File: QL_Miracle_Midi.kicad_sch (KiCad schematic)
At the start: 32 parts, among them J1 QL_cartridge_ROM, J2 DIN-5, J3 DIN-5, J4 DIN-5, U1 Z80CPU, U10 74LS74, U2 6264, U3 74LS374, U4 74LS374, U5 74LS10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

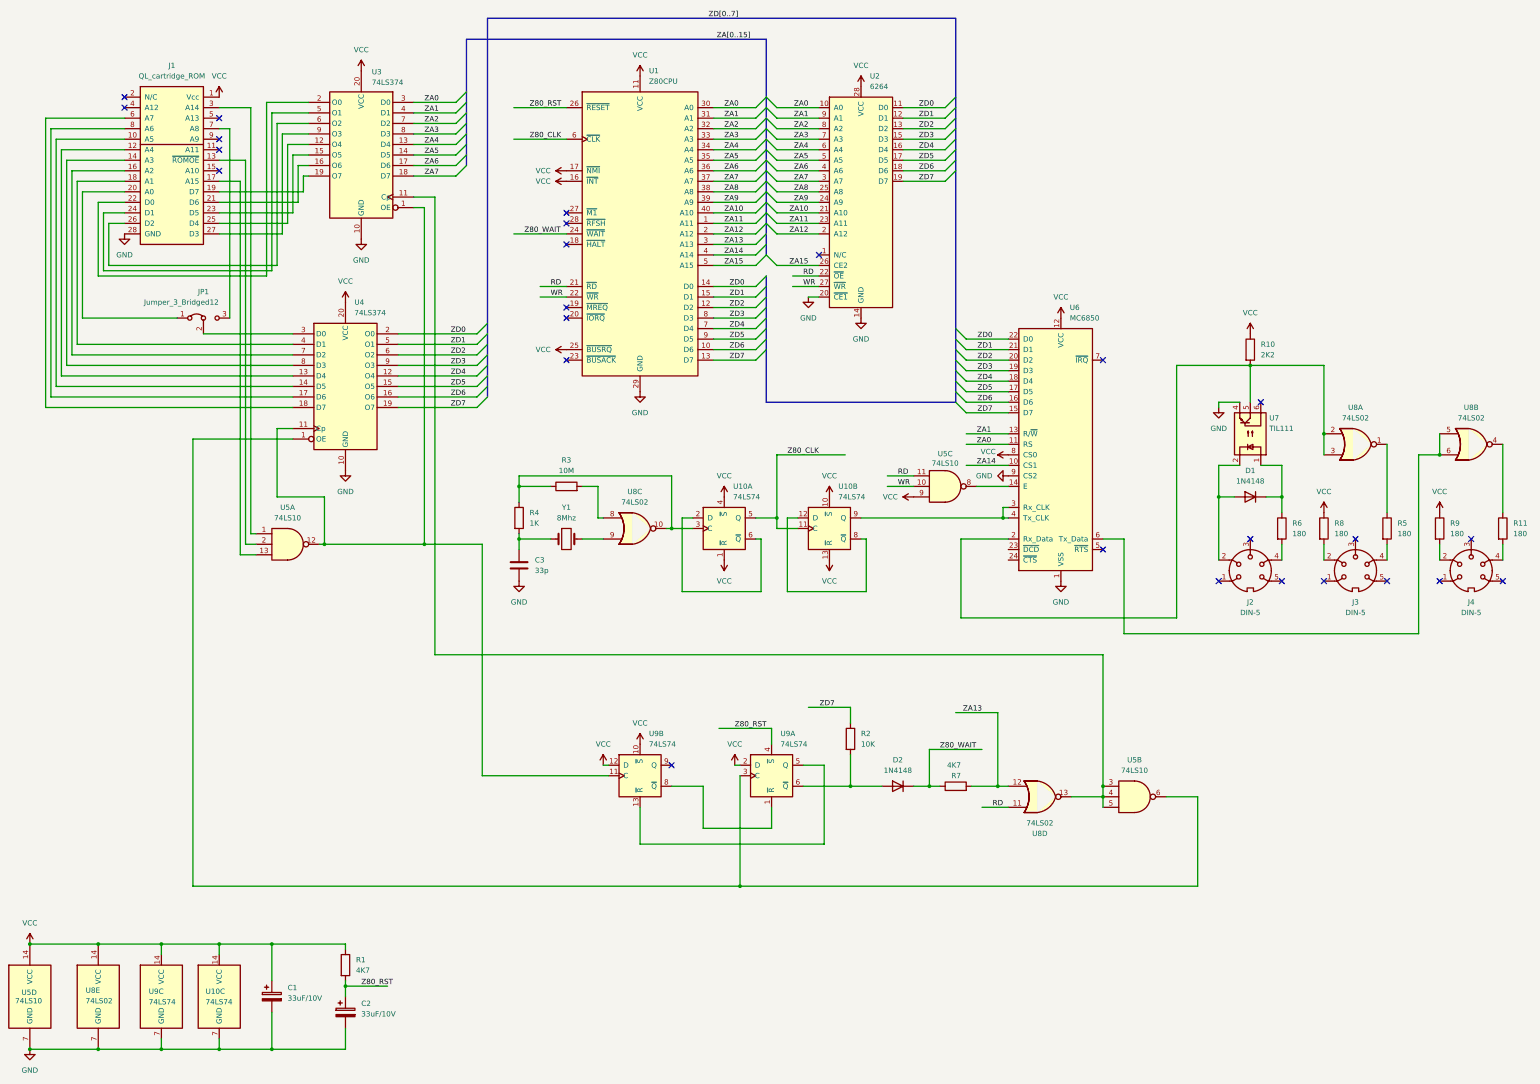
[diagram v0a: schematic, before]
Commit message: now based on real PCB
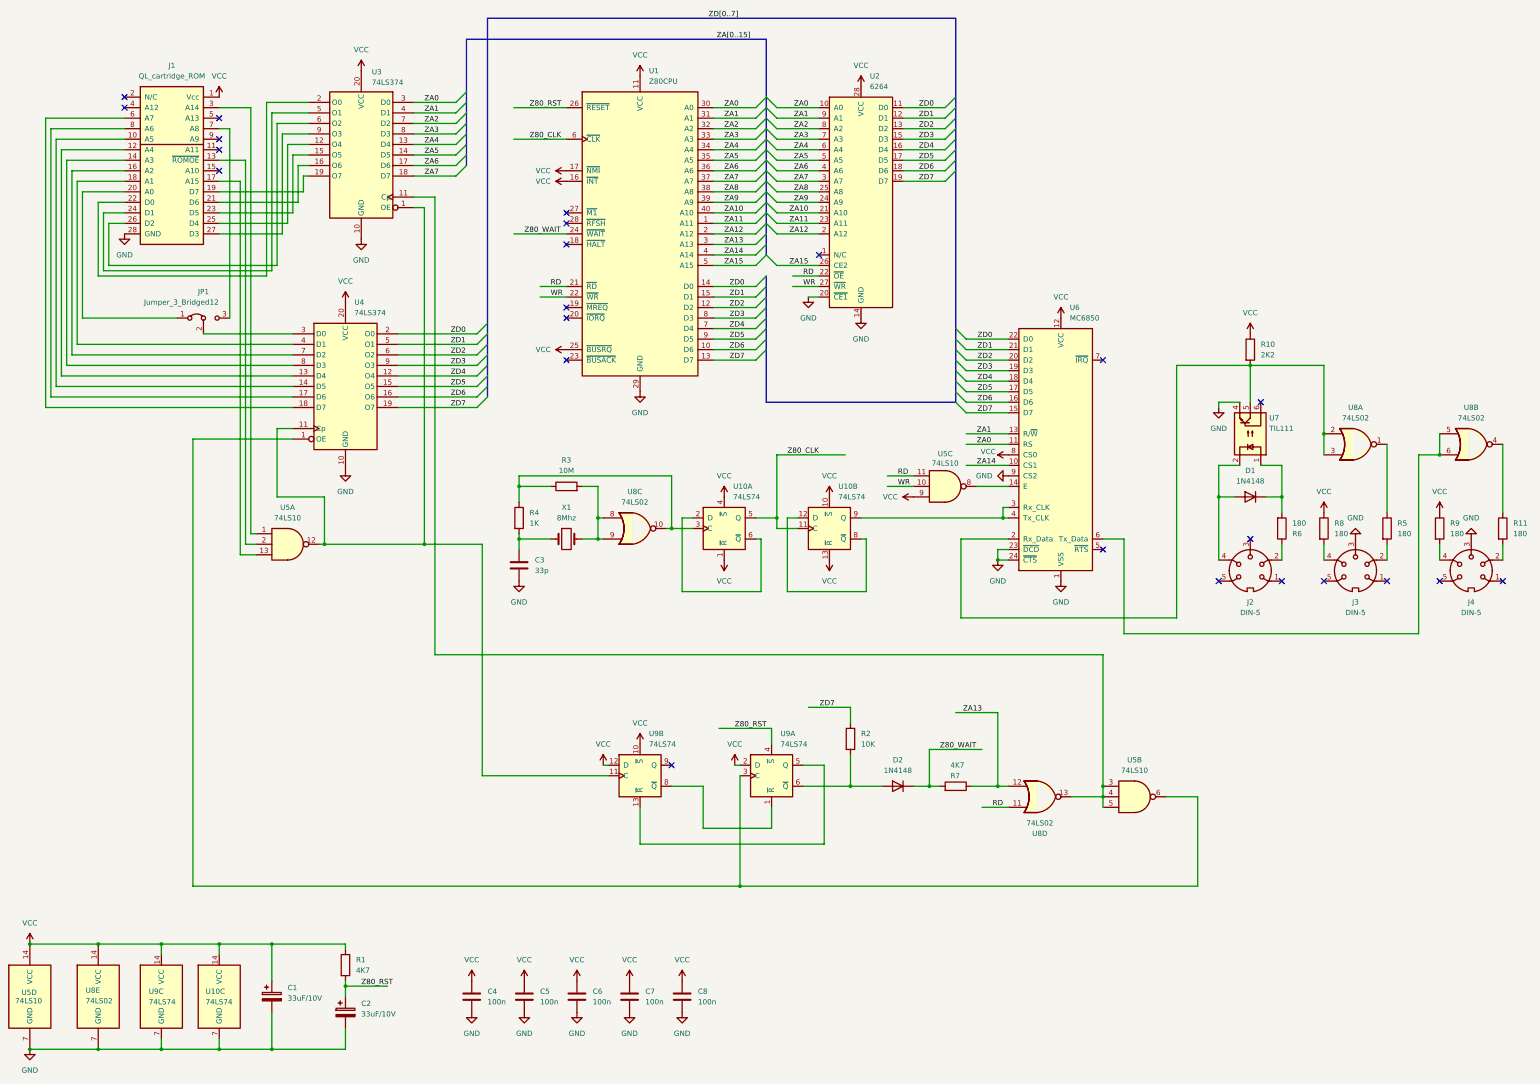
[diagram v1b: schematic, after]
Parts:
- added C4, C5, C6, C7, C8: 100n, Capacitor_THT:C_Disc_D4.3mm_W1.9mm_P5.00mm, symbol Device:C
- C1, C2: footprint Capacitor_THT:CP_Radial_D5.0mm_P2.50mm -> Capacitor_THT:CP_Axial_L11.0mm_D5.0mm_P18.00mm_Horizontal
- C3: footprint Capacitor_THT:C_Disc_D4.3mm_W1.9mm_P5.00mm -> Capacitor_THT:C_Disc_D3.8mm_W2.6mm_P2.50mm
- D1, D2: footprint Diode_THT:D_DO-35_SOD27_P7.62mm_Horizontal -> Diode_THT:D_DO-35_SOD27_P2.54mm_Vertical_KathodeUp
- J2, J3, J4: footprint 8bits:DIN-5-female-pcb-horizontal -> 8bits:DIN-5-female-pcb-horizontal-miracle
- R10, R11, R2, R3, R4, R5, R6, R7, R8, R9: footprint Resistor_THT:R_Axial_DIN0207_L6.3mm_D2.5mm_P10.16mm_Horizontal -> Resistor_THT:R_Axial_DIN0207_L6.3mm_D2.5mm_P2.54mm_Vertical
- U1: footprint Package_DIP:DIP-40_W15.24mm_Socket_LongPads -> Package_DIP:DIP-40_W15.24mm_Socket
- U10, U5, U8, U9: footprint Package_DIP:DIP-14_W7.62mm_Socket_LongPads -> Package_DIP:DIP-14_W7.62mm_Socket
- U2: footprint Package_DIP:DIP-28_W15.24mm_Socket_LongPads -> Package_DIP:DIP-28_W15.24mm_Socket
- U3, U4: footprint Package_DIP:DIP-20_W7.62mm_Socket_LongPads -> Package_DIP:DIP-20_W7.62mm_Socket
- U6: footprint Package_DIP:DIP-24_W15.24mm_Socket_LongPads -> Package_DIP:DIP-24_W15.24mm_Socket
- U7: footprint Package_DIP:DIP-6_W7.62mm_Socket_LongPads -> Package_DIP:DIP-6_W7.62mm_Socket
- renumbered Y1 to X1
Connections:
- net GND: now also J3.3, J4.3, U6.23 (~{DCD}), U6.24 (~{CTS}), C4.2, C5.2, C6.2, C7.2, C8.2
- net VCC: now also C4.1, C5.1, C6.1, C7.1, C8.1
- net Z80_WAIT: now also R7.2; no longer R7.1
- net ZA13: now also R7.1; no longer R7.2
- net at R3.2, U8.8: now also U8.9, X1.2
- net at R5.2: now also J3.2; no longer J3.4
- net at R11.2: now also J4.2; no longer J4.4
- net at D1.2 (A), U7.2: now also J2.4; no longer J2.2
- net at R6.2: now also D1.1 (K), U7.1; no longer J2.4
- net at R8.2: now also J3.4; no longer J3.2
- net at R9.2: now also J4.4; no longer J4.2
- new net: J2.2, R6.1
- no-connect marks 26 -> 24
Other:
- moved on the sheet: R7

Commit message: finish route
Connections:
- net GND: now also R8.1, R9.1
- net VCC: no longer R8.1, R9.1
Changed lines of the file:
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@@
 	)
 	(symbol
-		(lib_id "power:VCC")
-		(at 336.55 144.78 0)
+		(lib_id "power:GND")
+		(at 364.49 144.78 180)
 		(unit 1)
 		(exclude_from_sim no)
@@
 		(dnp no)
 		(fields_autoplaced yes)
-		(property "Reference" "#PWR015"
-			(at 336.55 148.59 0)
+		(property "Reference" "#PWR016"
+			(at 364.49 138.43 0)
 			(effects
 				(font
@@
 			)
 		)
-		(property "Value" "VCC"
-			(at 336.55 139.7 0)
+		(property "Value" "GND"
+			(at 364.49 139.7 0)
 			(effects
 				(font
@@
 		)
 		(property "Footprint" ""
-			(at 336.55 144.78 0)
+			(at 364.49 144.78 0)
 			(effects
 				(font
@@
 		)
 		(property "Datasheet" ""
-			(at 336.55 144.78 0)
+			(at 364.49 144.78 0)
 			(effects
 				(font
@@
 			)
 		)
-		(property "Description" "Power symbol creates a global label with name \"VCC\""
-			(at 336.55 144.78 0)
+		(property "Description" "Power symbol creates a global label with name \"GND\" , ground"
+			(at 364.49 144.78 0)
 			(effects
 				(font
@@
 			(project "QL_Miracle_Midi"
 				(path "/7208cd64-ad9c-4b78-9ce9-3e808fe0c4bf"
-					(reference "#PWR015")
+					(reference "#PWR016")
 					(unit 1)
 				)
@@
 	)
 	(symbol
+		(lib_id "power:GND")
+		(at 336.55 144.78 180)
+		(unit 1)
+		(exclude_from_sim no)
+		(in_bom yes)
+		(on_board yes)
+		(dnp no)
+		(fields_autoplaced yes)
+		(property "Reference" "#PWR015"
+			(at 336.55 138.43 0)
+			(effects
+				(font
+					(size 1.27 1.27)
+				)
+				(hide yes)
+			)
+		)
+		(property "Value" "GND"
+			(at 336.55 139.7 0)
+			(effects
+				(font
+					(size 1.27 1.27)
+				)
+			)
+		)
+		(property "Footprint" ""
+			(at 336.55 144.78 0)
+			(effects
+				(font
+					(size 1.27 1.27)
+				)
+				(hide yes)
+			)
+		)
+		(property "Datasheet" ""
+			(at 336.55 144.78 0)
+			(effects
+				(font
+					(size 1.27 1.27)
+				)
+				(hide yes)
+			)
+		)
+		(property "Description" "Power symbol creates a global label with name \"GND\" , ground"
+			(at 336.55 144.78 0)
+			(effects
+				(font
+					(size 1.27 1.27)
+				)
+				(hide yes)
+			)
+		)
+		(pin "1"
+		)
+		(instances
+			(project "QL_Miracle_Midi"
+				(path "/7208cd64-ad9c-4b78-9ce9-3e808fe0c4bf"
+					(reference "#PWR015")
+					(unit 1)
+				)
+			)
+		)
+	)
+	(symbol
 		(lib_id "Device:R")
 		(at 318.77 105.41 0)
@@
 					(unit 1)
 				)
-			)
-		)
-	)
-	(symbol
-		(lib_id "power:VCC")
-		(at 364.49 144.78 0)
-		(unit 1)
-		(exclude_from_sim no)
-		(in_bom yes)
-		(on_board yes)
-		(dnp no)
-		(fields_autoplaced yes)
-		(property "Reference" "#PWR016"
-			(at 364.49 148.59 0)
-			(effects
-				(font
-					(size 1.27 1.27)
-				)
-				(hide yes)
-			)
-		)
-		(property "Value" "VCC"
-			(at 364.49 139.7 0)
-			(effects
-				(font
-					(size 1.27 1.27)
-				)
-			)
-		)
-		(property "Footprint" ""
-			(at 364.49 144.78 0)
-			(effects
-				(font
-					(size 1.27 1.27)
-				)
-				(hide yes)
-			)
-		)
-		(property "Datasheet" ""
-			(at 364.49 144.78 0)
-			(effects
-				(font
-					(size 1.27 1.27)
-				)
-				(hide yes)
-			)
-		)
-		(property "Description" "Power symbol creates a global label with name \"VCC\""
-			(at 364.49 144.78 0)
-			(effects
-				(font
-					(size 1.27 1.27)
-				)
-				(hide yes)
-			)
-		)
-		(pin "1"
-		)
-		(instances
-			(project "QL_Miracle_Midi"
-				(path "/7208cd64-ad9c-4b78-9ce9-3e808fe0c4bf"
-					(reference "#PWR016")
-					(unit 1)
-				)
